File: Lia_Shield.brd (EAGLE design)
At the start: 58.2 x 33.6 mm, 8 parts, among them U1 HC_05

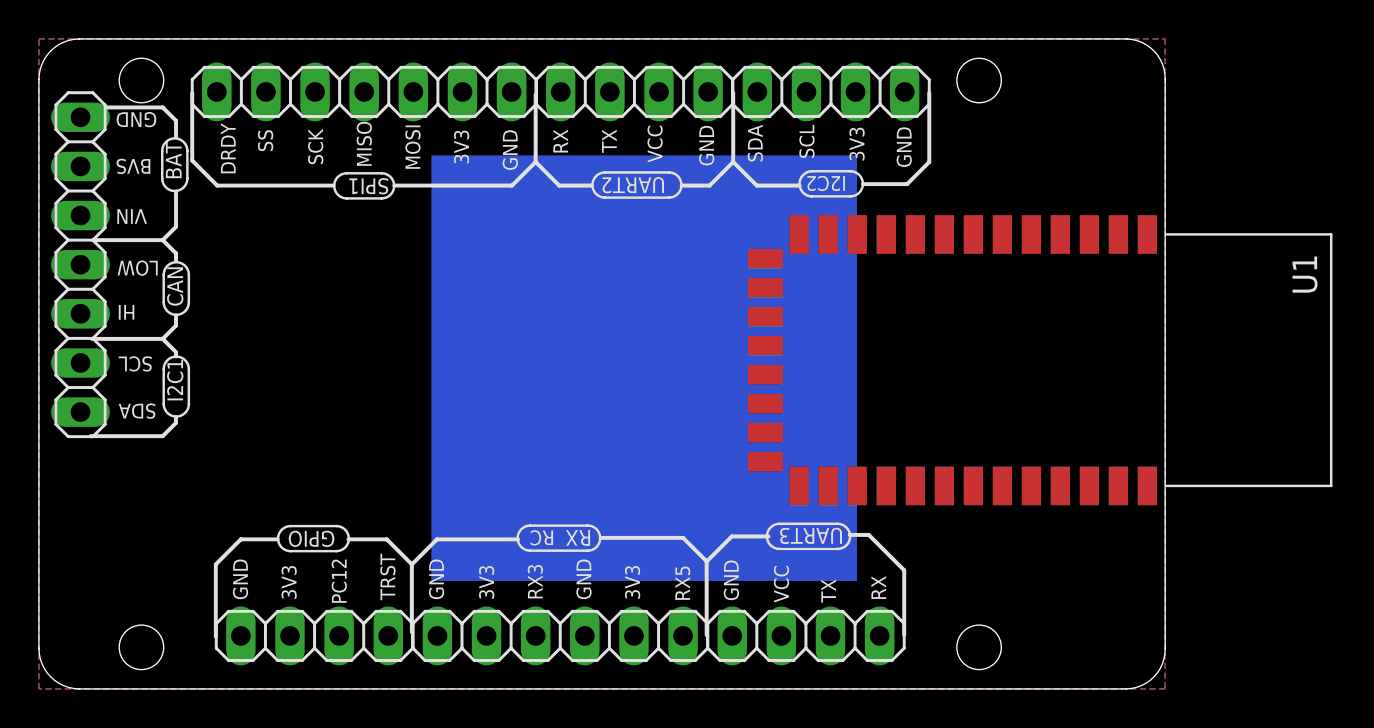
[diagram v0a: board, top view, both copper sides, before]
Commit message: angled receiver connector
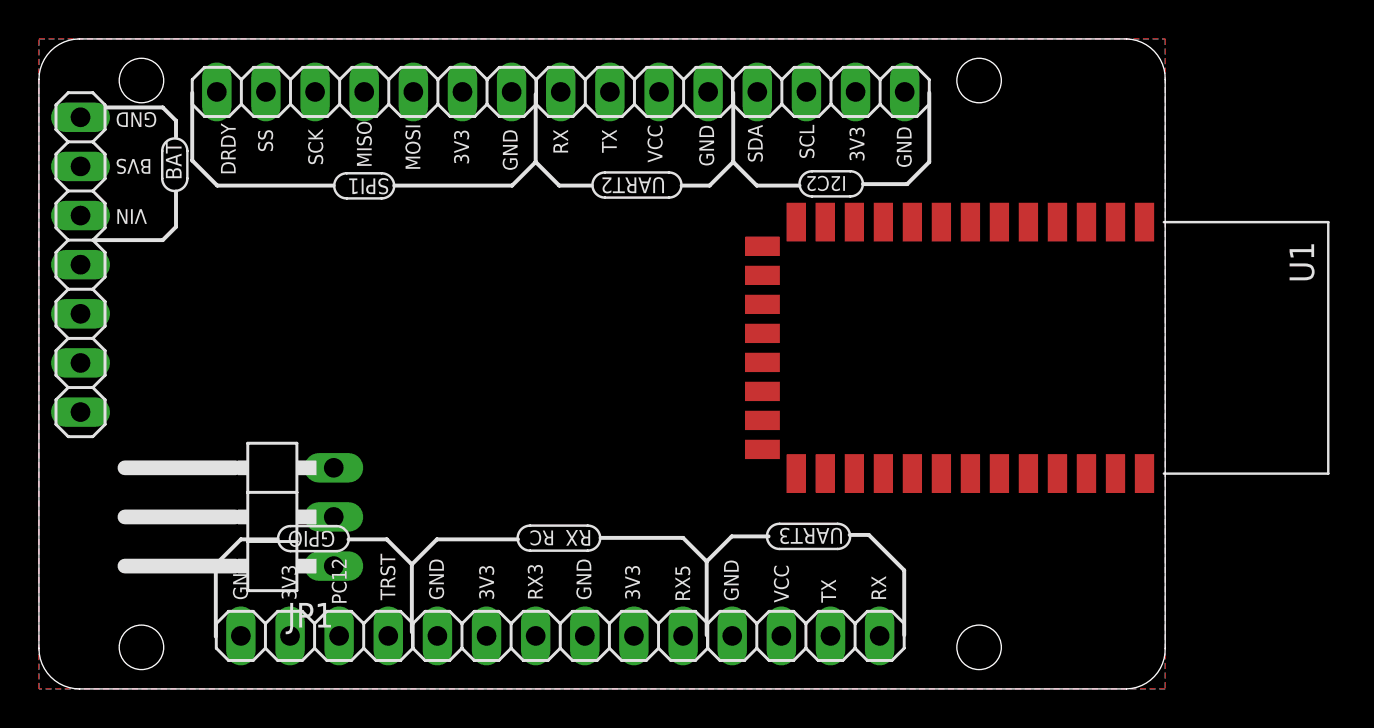
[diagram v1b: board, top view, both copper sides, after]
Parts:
- added JP1: (no value), pinhead:1X03/90
- moved U1 0.65 mm to (53.3, 17.8)
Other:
- board text removed: "(C) 2010-2011 Antoine Drouin <poinix@gmail.com>"
- board text removed: "(C) 2010-2012 Piotr Esden-Tempski <piotr@esden.net>"
- board text removed: "(C) 2011 Richard Hatano <rhatano@jobyenergy.com>"
- board text removed: "(C) 2011-2012 Transition Robotics <info@transition-robotics.com>"
- board text removed: "CAN"
- board text removed: "CC-BY-SA 3.0"
- board text removed: "HI"
- board text removed: "I2C1"
- board text removed: "LOW"
- board text removed: "Licensed under:"
- board text removed: "http://creativecommons.org/licenses/by-sa/3.0/"
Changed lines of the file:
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@@
 <setting verticaltext="up"/>
 </settings>
-<grid distance="3" unitdist="mil" unit="mm" style="dots" multiple="1" display="yes" altdistance="1" altunitdist="mil" altunit="mil"/>
+<grid distance="100" unitdist="mil" unit="mil" style="dots" multiple="1" display="yes" altdistance="50" altunitdist="mil" altunit="mil"/>
 <layers>
 <layer number="1" name="Top" color="4" fill="1" visible="yes" active="yes"/>
@@
 <wire x1="17.9828" y1="7.7314" x2="19.2782" y2="6.436" width="0.2032" layer="21"/>
 <wire x1="19.2782" y1="6.436" x2="19.2782" y2="2.9308" width="0.2032" layer="21"/>
-<wire x1="6.4004" y1="13.0654" x2="2.6666" y2="13.0654" width="0.2032" layer="21"/>
 <wire x1="24.7646" y1="7.7314" x2="20.5736" y2="7.7314" width="0.2032" layer="21"/>
 <wire x1="20.5736" y1="7.7314" x2="19.2782" y2="6.436" width="0.2032" layer="21"/>
@@
 <wire x1="44.8814" y1="26.0956" x2="46.0244" y2="27.2386" width="0.2032" layer="21"/>
 <wire x1="46.0244" y1="27.2386" x2="46.0244" y2="30.82" width="0.2032" layer="21"/>
-<wire x1="6.45" y1="14.73" x2="6.45" y2="16.53" width="0.127" layer="21"/>
-<wire x1="7.75" y1="16.53" x2="7.75" y2="14.73" width="0.127" layer="21"/>
-<wire x1="7.75" y1="16.53" x2="6.45" y2="16.53" width="0.127" layer="21" curve="180"/>
-<wire x1="6.45" y1="14.73" x2="7.75" y2="14.73" width="0.127" layer="21" curve="180"/>
-<wire x1="7.0862" y1="14.056" x2="7.0862" y2="13.7512" width="0.2032" layer="21"/>
-<wire x1="7.0862" y1="13.7512" x2="6.4004" y2="13.0654" width="0.2032" layer="21"/>
-<wire x1="2.7428" y1="18.0946" x2="6.4004" y2="18.0946" width="0.2032" layer="21"/>
-<wire x1="6.4004" y1="18.0946" x2="7.0862" y2="17.4088" width="0.2032" layer="21"/>
-<wire x1="7.0862" y1="17.4088" x2="7.0862" y2="17.1802" width="0.2032" layer="21"/>
-<wire x1="6.45" y1="19.9878" x2="6.45" y2="21.4068" width="0.127" layer="21"/>
-<wire x1="7.75" y1="21.4068" x2="7.75" y2="19.9878" width="0.127" layer="21"/>
-<wire x1="7.75" y1="21.4068" x2="6.45" y2="21.4068" width="0.127" layer="21" curve="180"/>
-<wire x1="6.45" y1="19.9878" x2="7.75" y2="19.9878" width="0.127" layer="21" curve="180"/>
-<wire x1="7.0862" y1="19.3138" x2="7.0862" y2="18.7804" width="0.2032" layer="21"/>
-<wire x1="7.0862" y1="18.7804" x2="6.4004" y2="18.0946" width="0.2032" layer="21"/>
 <wire x1="2.819" y1="23.2" x2="6.4004" y2="23.2" width="0.2032" layer="21"/>
-<wire x1="6.4004" y1="23.2" x2="7.0862" y2="22.5142" width="0.2032" layer="21"/>
-<wire x1="7.0862" y1="22.5142" x2="7.0862" y2="22.1332" width="0.2032" layer="21"/>
 <wire x1="6.3738" y1="26.3886" x2="6.3738" y2="27.8076" width="0.127" layer="21"/>
 <wire x1="7.6738" y1="27.8076" x2="7.6738" y2="26.3886" width="0.127" layer="21"/>
@@
 <text x="39.3188" y="29.1632" size="0.762" layer="21" font="vector" ratio="20" rot="R270">SCL</text>
 <text x="36.6518" y="29.1632" size="0.762" layer="21" font="vector" ratio="20" rot="R270">SDA</text>
-<text x="27.8488" y="-2.835" size="1.778" layer="49">Licensed under:</text>
 <text x="26.6696" y="8.1886" size="0.762" layer="21" font="vector" ratio="20" rot="SR180">RC</text>
-<text x="27.925" y="-6.5688" size="1.016" layer="49">http://creativecommons.org/licenses/by-sa/3.0/</text>
-<text x="0.6092" y="-3.3176" size="0.635" layer="49" ratio="20">(C) 2010-2011 Antoine Drouin &lt;poinix@gmail.com&gt;</text>
-<text x="0.6092" y="-4.4606" size="0.635" layer="49" ratio="20">(C) 2010-2012 Piotr Esden-Tempski &lt;piotr@esden.net&gt;</text>
-<text x="0.6092" y="-5.6036" size="0.635" layer="49" ratio="20">(C) 2011 Richard Hatano &lt;rhatano@jobyenergy.com&gt;</text>
-<text x="0.6092" y="-6.6704" size="0.635" layer="49" ratio="20">(C) 2011-2012 Transition Robotics &lt;info@transition-robotics.com&gt;</text>
-<text x="27.925" y="-5.121" size="1.778" layer="49">CC-BY-SA 3.0</text>
-<text x="6.6386" y="17.0904" size="0.8128" layer="21" font="vector" ratio="20" rot="R270">I2C1</text>
-<text x="6.6386" y="21.891" size="0.8128" layer="21" font="vector" ratio="20" rot="R270">CAN</text>
-<text x="4.1144" y="16.4182" size="0.762" layer="21" font="vector" ratio="20" rot="SR180" align="top-right">SCL</text>
-<text x="4.1144" y="13.9798" size="0.762" layer="21" font="vector" ratio="20" rot="SR180" align="top-right">SDA</text>
-<text x="4.0382" y="21.3712" size="0.762" layer="21" font="vector" ratio="20" rot="SR180" align="top-right">LOW</text>
-<text x="4.0382" y="19.0852" size="0.762" layer="21" font="vector" ratio="20" rot="SR180" align="top-right">HI</text>
 <text x="3.962" y="24.0382" size="0.762" layer="21" font="vector" ratio="20" rot="SR180" align="top-right">VIN</text>
 <text x="6.5624" y="28.2918" size="0.8128" layer="21" font="vector" ratio="20" rot="R270">BAT</text>
@@
 <hole x="48.6" y="31.45" drill="2.3"/>
 <hole x="48.6" y="2.15" drill="2.3"/>
-<rectangle x1="20.287" y1="5.5804" x2="42.287" y2="27.5804" layer="16"/>
 </plain>
 <attributes>
@@
 <attribute name="PARTNO" value="conn-th-0.1in-7-1" x="16.8144" y="30.86" size="1.778" layer="27" rot="R180" display="off"/>
 </element>
-<element name="U1" library="Bluetooth HC-05" package="BLUETOOTH_SMD" value="HC_05" x="53.4924" y="17.145" rot="R270"/>
+<element name="U1" library="Bluetooth HC-05" package="BLUETOOTH_SMD" value="HC_05" x="53.34" y="17.78" rot="R270"/>
+<element name="JP1" library="pinhead" package="1X03/90" value="" x="11.43" y="8.89" rot="R90"/>
 </elements>
 <signals>

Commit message: david wollte es so
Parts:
- added JP2, JP3: (no value), pinhead:1X06
- added R1, R2: (no value), rcl:R1206
- added S1: (no value), SparkFun-Electromechanical:TACTILE-PTH
- added VSENSE: (no value), pinhead:1X03/90
- JP21: device pinhead:1X07 -> pinhead:1X03
- moved JP21 5.08 mm to (2.15, 27.0)
- moved JP1 2.54 mm to (8.89, 8.89)
- moved U1 1.31 mm to (53.6, 16.5)
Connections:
- new net GND: R1.1
- new net N$1: JP21.2, VSENSE.1
- new net N$10: JP14.3, JP3.3, R2.2
- new net N$11: JP14.1, JP2.2, JP3.5
- new net N$12: JP14.2, JP2.3, JP3.4
- new net N$13: JP14.4, JP2.5, JP3.2
- new net N$14: JP15.4, JP3.1
- new net N$15: JP22.2, S1.3
- new net N$16: JP15.3, R1.2, S1.2
- new net N$17: JP2.4, R2.1
- new net N$2: JP1.1, JP20.1
- new net N$3: JP21.1, VSENSE.3
- new net N$4: JP17.1, U1.13
- new net N$5: JP1.2, JP20.2
- new net N$6: JP1.3, JP20.3
- new net N$7: JP17.2, U1.12
- new net N$8: JP17.3, U1.2
- new net N$9: JP17.4, U1.1
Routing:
- net N$9: track 0.00 -> 37.8 mm
- net N$13: track 0.00 -> 35.9 mm
- net N$8: track 0.00 -> 35.5 mm
- net N$16: track 0.00 -> 34.3 mm
- net N$10: track 0.00 -> 28.9 mm
- net N$7: track 0.00 -> 23.1 mm
- net N$6: track 0.00 -> 17.2 mm
- net N$15: track 0.00 -> 15.6 mm
- net N$5: track 0.00 -> 13.3 mm
- net N$2: track 0.00 -> 10.2 mm

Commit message: comitting scheiß
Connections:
- removed net N$11: JP14.1, JP2.2, JP3.5
- removed net N$12: JP14.2, JP2.3, JP3.4
- removed net N$15: JP22.2, S1.3
- removed net N$2 (its old number): JP1.1, JP20.1
- removed net N$3: JP21.1, VSENSE.3
- removed net N$4: JP17.1, U1.13
- removed net N$5: JP1.2, JP20.2
- removed net N$7: JP17.2, U1.12
- new net RC1: JP14.1, JP17.1, JP2.2, JP21.1, JP3.5, R1.1, U1.13, VSENSE.3
- new net VCC: JP1.2, JP14.2, JP16.2, JP17.2, JP2.3, JP20.2, JP20.5, JP22.2, JP3.4, S1.3, U1.12
- net GND: now also JP1.1, JP20.1, JP20.4; no longer R1.1
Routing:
- net VCC: track 0.00 -> 56.7 mm
- net N$7: track 23.1 -> 0.00 mm
- net N$1: track 0.00 -> 18.4 mm
- net N$15: track 15.6 -> 0.00 mm
- net N$5: track 13.3 -> 0.00 mm
- net N$2 (its old number): track 10.2 -> 0.00 mm
- net N$17: track 0.00 -> 9.31 mm
- net RC1: track 0.00 -> 9.11 mm
- net N$8: track 35.5 -> 38.4 mm
- net N$10: track 28.9 -> 30.2 mm
- net N$9: track 37.8 -> 38.7 mm
- added copper zone on layer 1, net RC1
- added copper zone on layer 16, net RC1
- added copper zone on layer 2, net RC1
- removed copper zone on layer 1, net GND
- removed copper zone on layer 16, net GND
- removed copper zone on layer 2, net GND
